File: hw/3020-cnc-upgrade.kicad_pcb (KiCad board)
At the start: 2 copper layers, 69 x 29 mm, 14 parts, among them P1 CONN_01X02, P2 CONN_01X03, P3 CONN_01X08, P4 CONN_01X03, U1 6N136, U2 arduino_pro_micro, U3 MCP41010

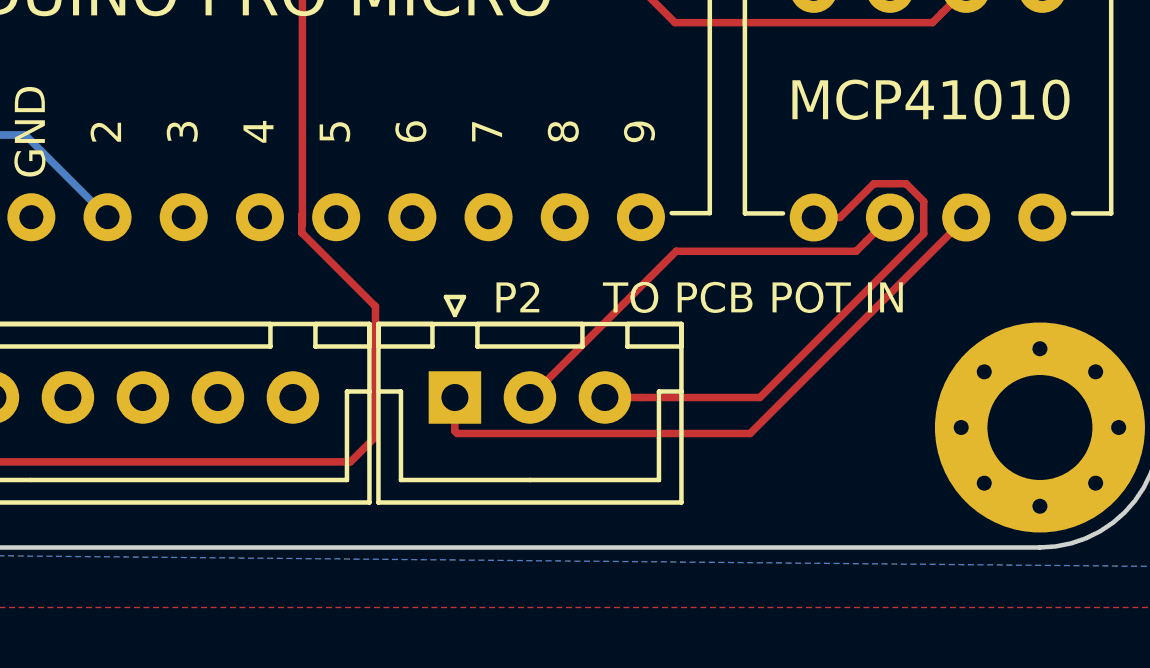
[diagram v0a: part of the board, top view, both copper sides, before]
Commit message: added jumper to reverse spindle polarity
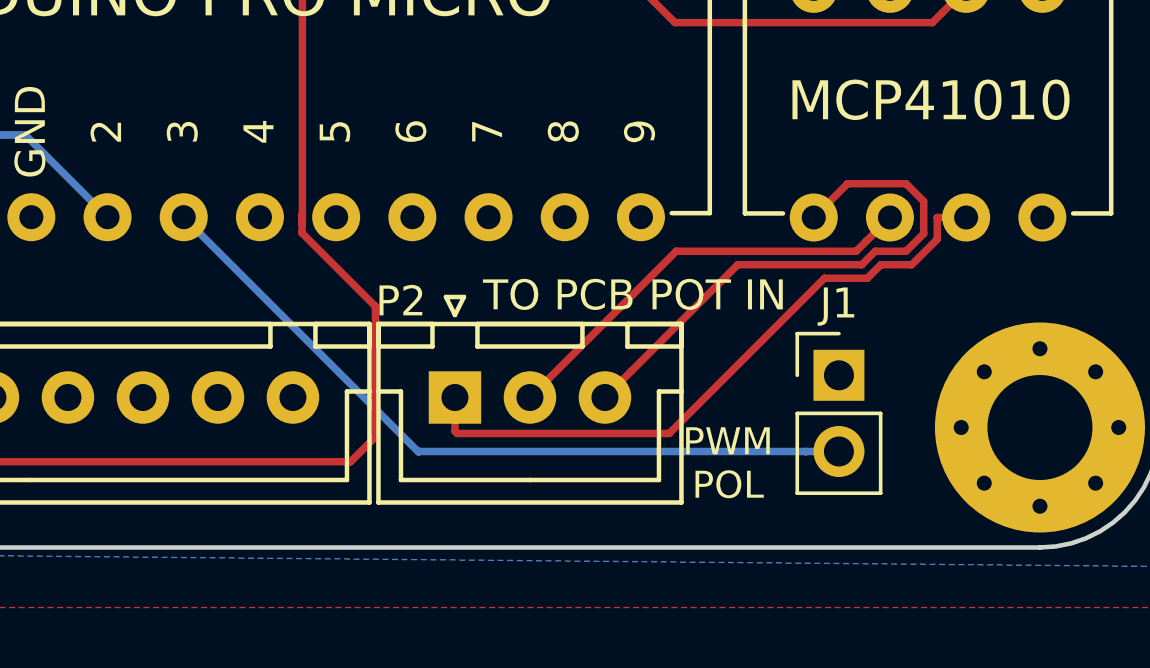
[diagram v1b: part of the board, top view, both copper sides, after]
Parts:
- added J1: CONN_01X02, Pin_Headers:Pin_Header_Straight_1x02_Pitch2.54mm, F.Cu at (177.3, 112.3)
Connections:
- U2 pad 6: Net-(U2-Pad6) -> /pol
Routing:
- net /pol: track 0.00 -> 25.1 mm
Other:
- board text added: "PWM POL"
